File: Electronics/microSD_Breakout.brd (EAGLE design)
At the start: 21.8 x 26.9 mm, 2 parts, among them U1 USD-SOCKETUSD

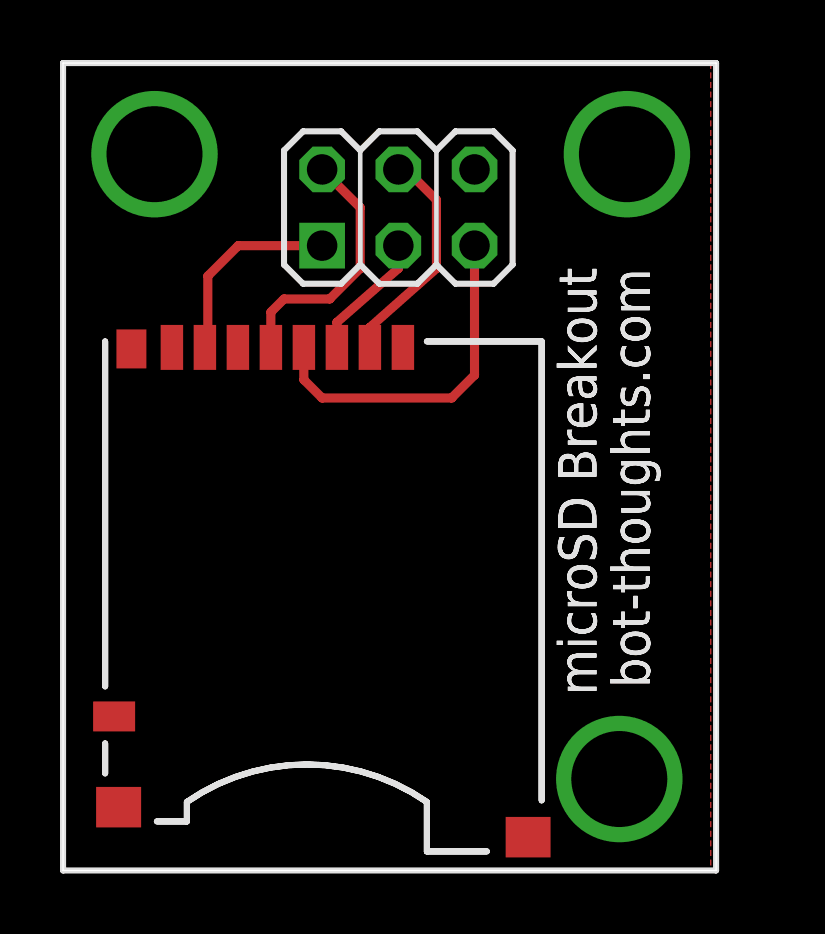
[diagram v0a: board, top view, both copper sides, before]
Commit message: Moved RC Mux to subdirectory. Minor changes to various other boards.
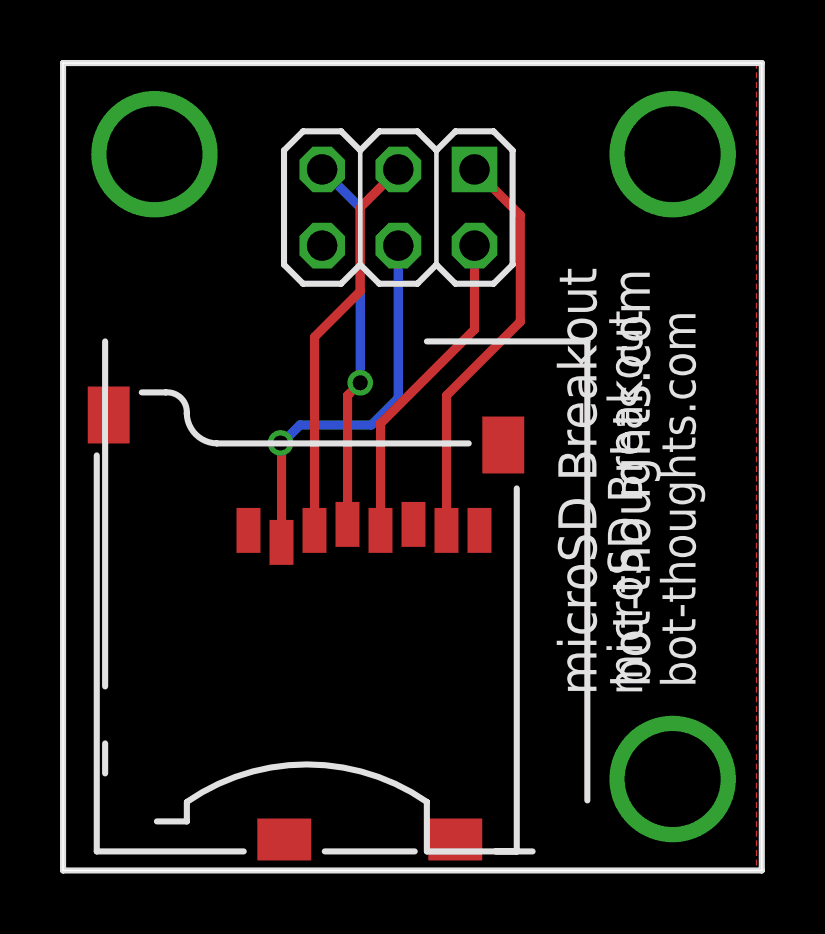
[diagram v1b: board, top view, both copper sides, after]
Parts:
- U1: value USD-SOCKETUSD -> USD-SOCKETNEW; device SparkFun:USD-SOCKET-PP -> SparkFun:MICRO-SD-SOCKET-PP
- moved U1 7.00 mm to (15.1, 0.64)
- turned JP1 to 180 degrees
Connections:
- net GND: now also U1.GND3; no longer U1.GND2
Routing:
- net DI: track 4.32 -> 13.2 mm
- net DO: track 6.71 -> 13.7 mm
- net !CS: track 7.35 -> 13.0 mm, vias 0 -> 1
- net SCK: track 8.59 -> 10.8 mm
- net VCC: track 11.7 -> 12.5 mm, vias 0 -> 1
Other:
- board size 21.8 x 26.9 mm -> 23.3 x 26.9 mm
- board text added: "Rev 0.2"
